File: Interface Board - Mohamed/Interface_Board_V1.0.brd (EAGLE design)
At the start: 118.1 x 87.6 mm, 29 parts, among them IC1 4066N, IC2 4066N

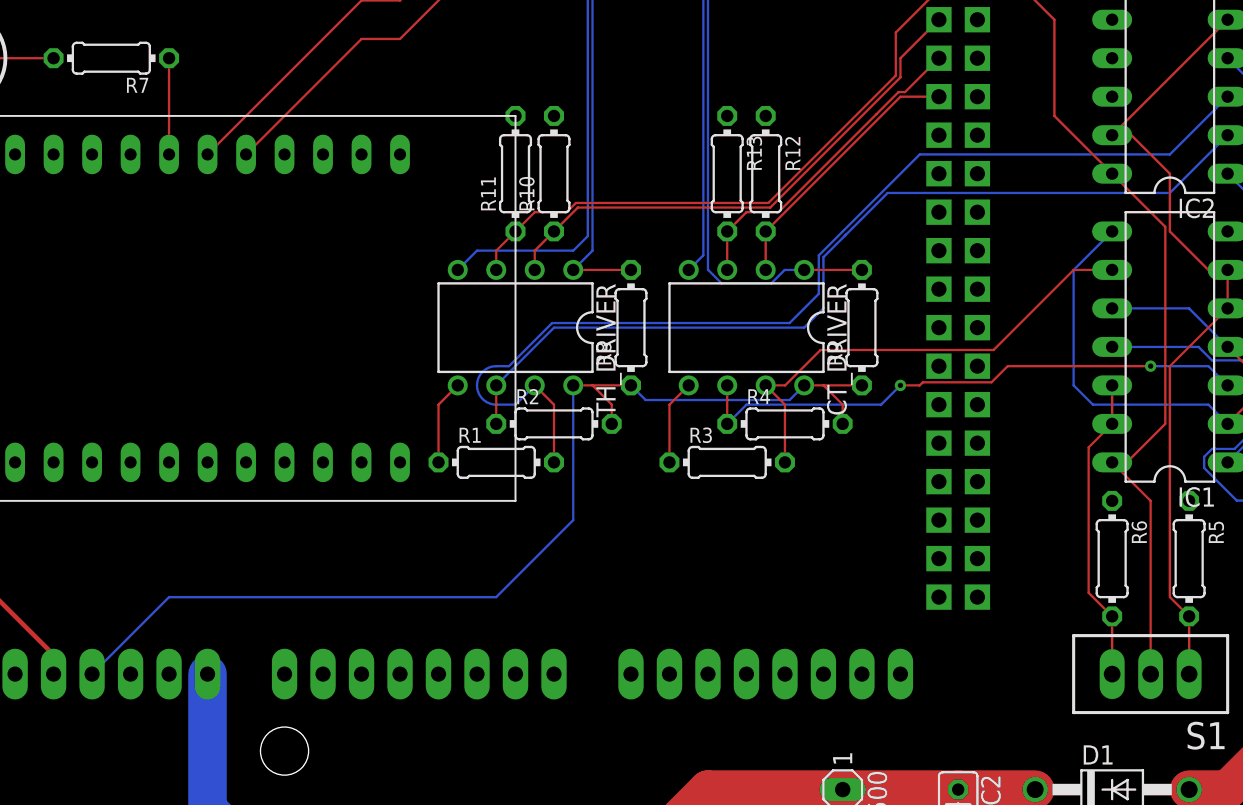
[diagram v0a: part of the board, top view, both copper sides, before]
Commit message: Fixed some VCC issues & added digital control signals for the kill switch
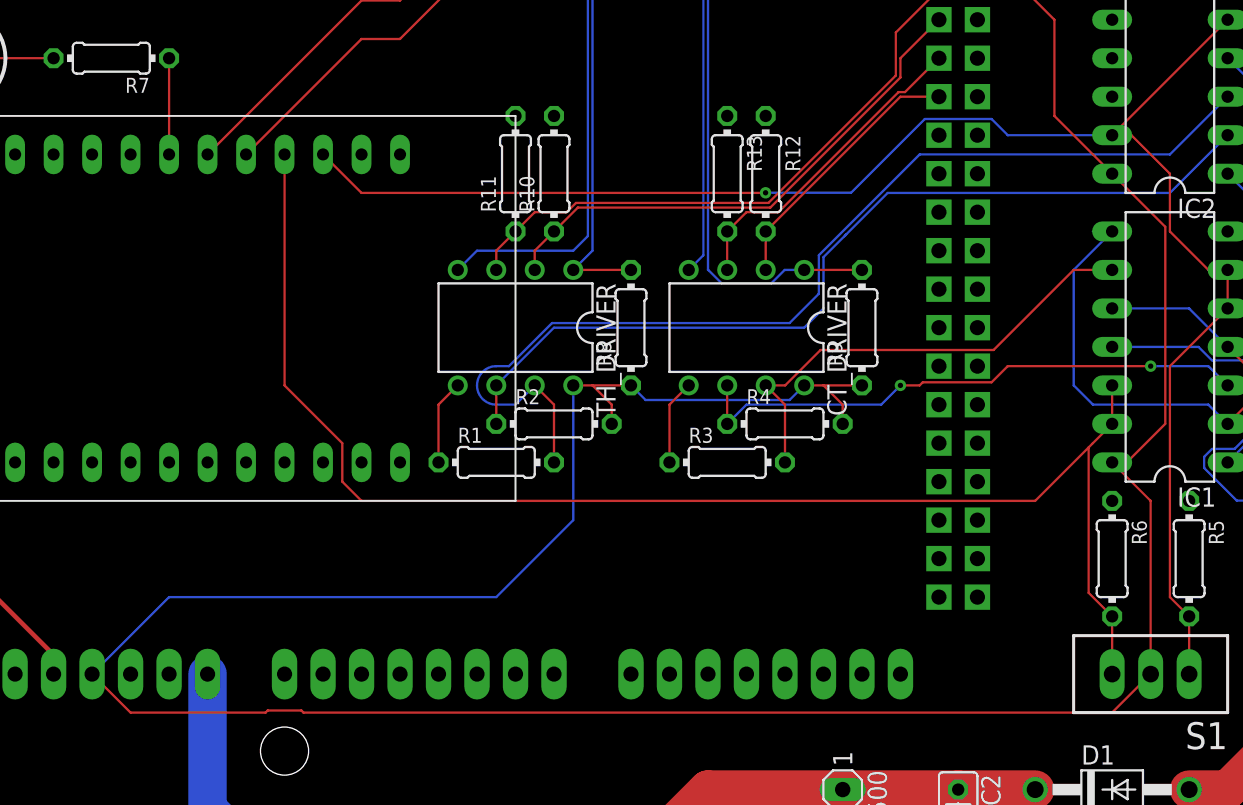
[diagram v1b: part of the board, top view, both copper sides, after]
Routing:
- net BYPASS_SIG: track 20.3 -> 94.7 mm
- net VCC: track 129.8 -> 201.9 mm
- net PASS_SIG: track 53.1 -> 108.7 mm, vias 0 -> 1
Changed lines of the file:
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@@
 <wire x1="58.1152" y1="48.5648" x2="57.15" y2="49.53" width="0.1524" layer="16"/>
 <wire x1="67.6148" y1="48.5648" x2="58.1152" y2="48.5648" width="0.1524" layer="16"/>
-<wire x1="72.39" y1="49.53" x2="88.9" y2="44.45" width="0" layer="19" extent="1-1"/>
+<wire x1="21.59" y1="30.48" x2="24.13" y2="27.94" width="0.1524" layer="1"/>
+<wire x1="88.9" y1="27.94" x2="91.44" y2="30.48" width="0.1524" layer="1"/>
+<wire x1="24.13" y1="27.94" x2="33.04033125" y2="27.94" width="0.1524" layer="1"/>
+<wire x1="33.04033125" y1="27.94" x2="33.18003125" y2="28.0797" width="0.1524" layer="1"/>
+<wire x1="33.18003125" y1="28.0797" x2="35.39996875" y2="28.0797" width="0.1524" layer="1"/>
+<wire x1="35.39996875" y1="28.0797" x2="35.53966875" y2="27.94" width="0.1524" layer="1"/>
+<wire x1="35.53966875" y1="27.94" x2="88.9" y2="27.94" width="0.1524" layer="1"/>
 </signal>
 <signal name="BYPASS_SIG">
@@
 <wire x1="88.9" y1="46.99" x2="88.9" y2="49.53" width="0.1524" layer="1"/>
 <wire x1="88.9" y1="30.48" x2="88.9" y2="34.29" width="0.1524" layer="1"/>
-<wire x1="88.9" y1="46.99" x2="87.3506" y2="45.4406" width="0.1524" layer="1"/>
+<wire x1="88.9" y1="46.99" x2="87.63" y2="45.72" width="0.1524" layer="1"/>
+<wire x1="87.63" y1="45.72" x2="87.3506" y2="45.4406" width="0.1524" layer="1"/>
 <wire x1="87.3506" y1="35.8394" x2="88.9" y2="34.29" width="0.1524" layer="1"/>
 <wire x1="87.3506" y1="45.4406" x2="87.3506" y2="35.8394" width="0.1524" layer="1"/>
-<wire x1="34.29" y1="64.77" x2="87.3506" y2="45.4406" width="0" layer="19" extent="1-1"/>
+<wire x1="34.29" y1="64.77" x2="34.29" y2="49.53" width="0.1524" layer="1"/>
+<wire x1="34.29" y1="49.53" x2="38.1" y2="45.72" width="0.1524" layer="1"/>
+<wire x1="38.1" y1="45.72" x2="38.1" y2="43.18" width="0.1524" layer="1"/>
+<wire x1="38.1" y1="43.18" x2="39.37" y2="41.91" width="0.1524" layer="1"/>
+<wire x1="39.37" y1="41.91" x2="83.82" y2="41.91" width="0.1524" layer="1"/>
+<wire x1="83.82" y1="41.91" x2="87.3506" y2="45.4406" width="0.1524" layer="1"/>
 </signal>
 <signal name="B_TH">
@@
 <wire x1="96.52" y1="68.58" x2="92.71" y2="64.77" width="0.1524" layer="16"/>
 <wire x1="92.71" y1="64.77" x2="76.2" y2="64.77" width="0.1524" layer="16"/>
-<wire x1="76.2" y1="64.77" x2="71.12" y2="59.69" width="0.1524" layer="16"/>
-<wire x1="69.85" y1="35.56" x2="69.85" y2="35.56" width="0.1524" layer="16"/>
-<wire x1="69.5452" y1="58.1152" x2="69.5452" y2="55.88" width="0.1524" layer="16"/>
-<wire x1="71.12" y1="59.69" x2="69.5452" y2="58.1152" width="0.1524" layer="16"/>
-<wire x1="69.5452" y1="55.88" x2="69.5452" y2="55.5752" width="0.1524" layer="16"/>
+<wire x1="76.2" y1="64.77" x2="69.5452" y2="58.1152" width="0.1524" layer="16"/>
+<wire x1="69.5452" y1="58.1152" x2="69.5452" y2="55.5752" width="0.1524" layer="16"/>
 <wire x1="69.5452" y1="55.5752" x2="67.6148" y2="53.6448" width="0.1524" layer="16"/>
 <wire x1="48.26" y1="50.8" x2="49.09894375" y2="50.8" width="0.1524" layer="16"/>
@@
 <wire x1="48.26" y1="48.26" x2="49.53" y2="48.26" width="0.1524" layer="16"/>
 <wire x1="49.53" y1="48.26" x2="50.8" y2="49.53" width="0.1524" layer="16"/>
-<wire x1="67.6148" y1="53.6448" x2="69.85" y2="35.56" width="0" layer="19" extent="16-16"/>
 </signal>
 <signal name="A_TH_DRIVER">
@@
 <wire x1="92.71" y1="50.8" x2="92.71" y2="35.56" width="0.1524" layer="1"/>
 <wire x1="92.71" y1="35.56" x2="93.98" y2="34.29" width="0.1524" layer="1"/>
-<wire x1="36.83" y1="64.77" x2="88.9" y2="66.04" width="0" layer="19" extent="1-1"/>
+<wire x1="36.83" y1="64.77" x2="39.37" y2="62.23" width="0.1524" layer="1"/>
+<wire x1="39.37" y1="62.23" x2="66.02079375" y2="62.23" width="0.1524" layer="1"/>
+<wire x1="66.02079375" y1="62.23" x2="66.030396875" y2="62.239603125" width="0.1524" layer="1"/>
+<via x="66.030396875" y="62.239603125" extent="1-16" drill="0.35"/>
+<wire x1="66.030396875" y1="62.239603125" x2="71.669915625" y2="62.239603125" width="0.1524" layer="16"/>
+<wire x1="80.9428875" y1="67.1068" x2="82.0096875" y2="66.04" width="0.1524" layer="16"/>
+<wire x1="82.0096875" y1="66.04" x2="88.9" y2="66.04" width="0.1524" layer="16"/>
+<wire x1="71.669915625" y1="62.239603125" x2="76.5371125" y2="67.1068" width="0.1524" layer="16"/>
+<wire x1="76.5371125" y1="67.1068" x2="80.9428875" y2="67.1068" width="0.1524" layer="16"/>
 </signal>
 <signal name="A_CT_DRIVER">
@@
 <wire x1="63.5" y1="59.69" x2="64.77" y2="60.96" width="0.1524" layer="1"/>
 <wire x1="64.77" y1="60.96" x2="66.87894375" y2="60.96" width="0.1524" layer="1"/>
-<wire x1="66.87894375" y1="60.96" x2="73.3552" y2="67.43625625" width="0.1524" layer="1"/>
+<wire x1="66.87894375" y1="60.96" x2="74.80374375" y2="68.8848" width="0.1524" layer="1"/>
 <contactref element="U$1" pad="D26"/>
-<wire x1="72.0852" y1="43.30625625" x2="72.0852" y2="43.30625625" width="0.1524" layer="1"/>
 <wire x1="77.47" y1="71.12" x2="75.2348" y2="68.8848" width="0.1524" layer="1"/>
-<wire x1="74.80374375" y1="68.8848" x2="73.3552" y2="67.43625625" width="0.1524" layer="1"/>
 <wire x1="75.2348" y1="68.8848" x2="74.80374375" y2="68.8848" width="0.1524" layer="1"/>
-<wire x1="72.0852" y1="43.30625625" x2="63.5" y2="57.15" width="0" layer="19" extent="1-1"/>
 </signal>
 <signal name="CT_TX">
